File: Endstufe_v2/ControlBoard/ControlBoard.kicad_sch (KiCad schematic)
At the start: 20 parts, among them J1 B4B-XH-2_(LF)(SN), J15 B4B-XH-2_(LF)(SN), J16 B6B-XH-2(LF)(SN), J2 B4B-XH-2_(LF)(SN), J20 DNP, J21 DNP, J3 B4B-XH-2_(LF)(SN), J4 DNP, J5 B6B-XH-2(LF)(SN)

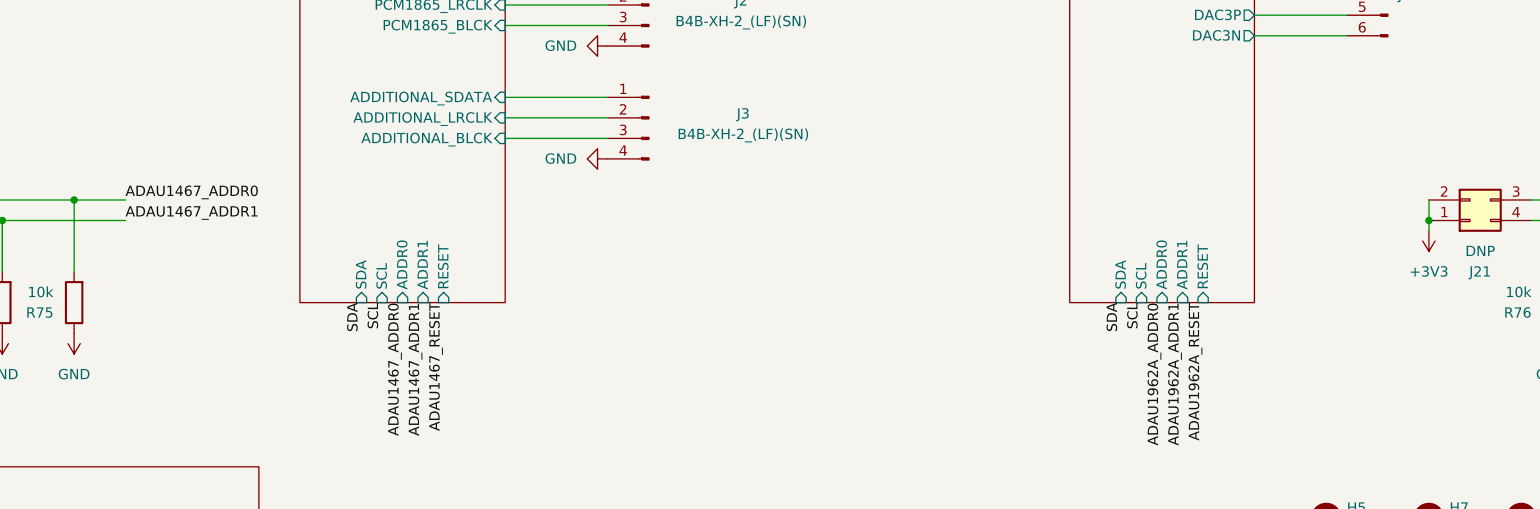
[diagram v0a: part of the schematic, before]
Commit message: Add information about I2C Addresses
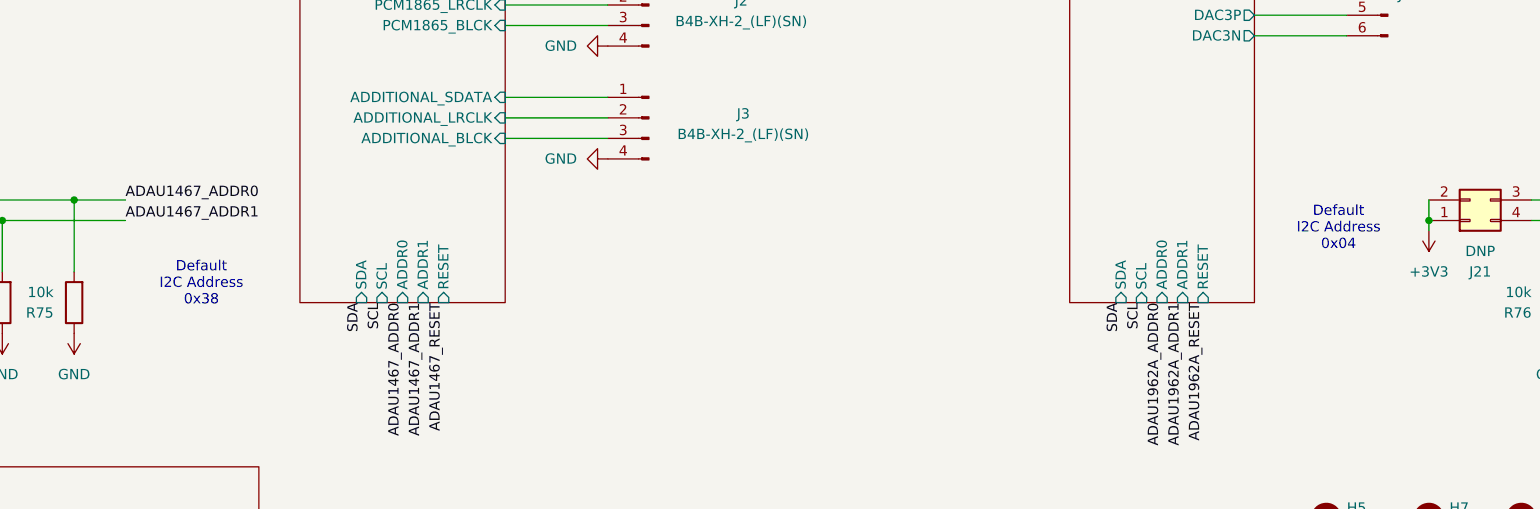
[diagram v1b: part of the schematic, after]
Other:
- note added: "Default I2C Address 0x04"
- note added: "Default I2C Address 0x38"
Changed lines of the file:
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@@
+		)
+	)
+	(text "Default\nI2C Address\n0x38"
+		(exclude_from_sim no)
+		(at 70.358 106.934 0)
+		(effects
+			(font
+				(size 1.27 1.27)
+			)
+		)
+	)
+	(text "Default\nI2C Address\n0x04"
+		(exclude_from_sim no)
+		(at 211.074 100.076 0)
+		(effects
+			(font
+				(size 1.27 1.27)
+			)
 		)
 	)

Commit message: Change unavailable parts to available ones, optimise silkscreen, do via stiching
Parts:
- J1, J15, J2, J3: footprint Endstufe:CONN-TH_B4B-XH-2-LF-SN -> Endstufe:JST_XH_B4B-XH-A_1x04_P2.50mm_Vertical; JLCPCB Position Offset (none) -> 0,-0.5
- J16, J5: footprint Endstufe:CONN-TH_B6B-XH-2-LF-SN -> Endstufe:JST_XH_B6B-XH-A_1x06_P2.50mm_Vertical; JLCPCB Position Offset (none) -> 0,-0.5
- J20, J21: footprint Connector_PinHeader_2.54mm:PinHeader_2x02_P2.54mm_Vertical -> Endstufe:PinHeader_2x02_P2.54mm_Vertical
- J4: footprint Connector_PinHeader_2.54mm:PinHeader_1x06_P2.54mm_Vertical -> Endstufe:PinHeader_1x06_P2.54mm_Vertical
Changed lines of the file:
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@@
 			)
 		)
-		(property "Footprint" "Endstufe:CONN-TH_B4B-XH-2-LF-SN"
+		(property "Footprint" "Endstufe:JST_XH_B4B-XH-A_1x04_P2.50mm_Vertical"
 			(at 125.73 68.58 0)
 			(effects
@@
 		(property "LCSC" "C157999"
 			(at 125.476 75.946 0)
+			(effects
+				(font
+					(size 1.27 1.27)
+				)
+				(hide yes)
+			)
+		)
+		(property "JLCPCB Position Offset" "0,-0.5"
+			(at 251.46 116.84 0)
 			(effects
 				(font
@@
 			)
 		)
-		(property "Footprint" "Endstufe:CONN-TH_B4B-XH-2-LF-SN"
+		(property "Footprint" "Endstufe:JST_XH_B4B-XH-A_1x04_P2.50mm_Vertical"
 			(at 125.73 82.55 0)
 			(effects
@@
 		(property "LCSC" "C157999"
 			(at 125.476 89.916 0)
+			(effects
+				(font
+					(size 1.27 1.27)
+				)
+				(hide yes)
+			)
+		)
+		(property "JLCPCB Position Offset" "0,-0.5"
+			(at 251.46 144.78 0)
 			(effects
 				(font
@@
 			)
 		)
-		(property "Footprint" "Endstufe:CONN-TH_B6B-XH-2-LF-SN"
+		(property "Footprint" "Endstufe:JST_XH_B6B-XH-A_1x06_P2.50mm_Vertical"
 			(at 217.17 68.58 0)
 			(effects
@@
 		(property "LCSC" "C157986"
 			(at 217.17 68.58 0)
+			(effects
+				(font
+					(size 1.27 1.27)
+				)
+				(hide yes)
+			)
+		)
+		(property "JLCPCB Position Offset" "0,-0.5"
+			(at 434.34 137.16 0)
 			(effects
 				(font
@@
 			)
 		)
-		(property "Footprint" "Connector_PinHeader_2.54mm:PinHeader_1x06_P2.54mm_Vertical"
+		(property "Footprint" "Endstufe:PinHeader_1x06_P2.54mm_Vertical"
 			(at 143.51 24.13 0)
 			(effects
@@
 			)
 		)
-		(property "Footprint" "Endstufe:CONN-TH_B6B-XH-2-LF-SN"
+		(property "Footprint" "Endstufe:JST_XH_B6B-XH-A_1x06_P2.50mm_Vertical"
 			(at 116.84 152.4 0)
 			(effects
@@
 		(property "LCSC" "C157986"
 			(at 116.84 152.4 0)
+			(effects
+				(font
+					(size 1.27 1.27)
+				)
+				(hide yes)
+			)
+		)
+		(property "JLCPCB Position Offset" "0,-0.5"
+			(at 233.68 304.8 0)
 			(effects
 				(font
@@
 			)
 		)
-		(property "Footprint" "Endstufe:CONN-TH_B4B-XH-2-LF-SN"
+		(property "Footprint" "Endstufe:JST_XH_B4B-XH-A_1x04_P2.50mm_Vertical"
 			(at 125.73 96.52 0)
 			(effects
@@
 		(property "LCSC" "C157999"
 			(at 125.476 103.886 0)
+			(effects
+				(font
+					(size 1.27 1.27)
+				)
+				(hide yes)
+			)
+		)
+		(property "JLCPCB Position Offset" "0,-0.5"
+			(at 251.46 172.72 0)
 			(effects
 				(font
@@
 			)
 		)
-		(property "Footprint" "Connector_PinHeader_2.54mm:PinHeader_2x02_P2.54mm_Vertical"
+		(property "Footprint" "Endstufe:PinHeader_2x02_P2.54mm_Vertical"
 			(at 227.33 99.06 0)
 			(effects
@@
 			)
 		)
-		(property "Footprint" "Endstufe:CONN-TH_B4B-XH-2-LF-SN"
+		(property "Footprint" "Endstufe:JST_XH_B4B-XH-A_1x04_P2.50mm_Vertical"
 			(at 116.84 175.26 0)
 			(effects
@@
 		(property "LCSC" "C157999"
 			(at 116.586 182.626 0)
+			(effects
+				(font
+					(size 1.27 1.27)
+				)
+				(hide yes)
+			)
+		)
+		(property "JLCPCB Position Offset" "0,-0.5"
+			(at 233.68 330.2 0)
 			(effects
 				(font
@@
 			)
 		)
-		(property "Footprint" "Connector_PinHeader_2.54mm:PinHeader_2x02_P2.54mm_Vertical"
+		(property "Footprint" "Endstufe:PinHeader_2x02_P2.54mm_Vertical"
 			(at 35.56 99.06 0)
 			(effects
